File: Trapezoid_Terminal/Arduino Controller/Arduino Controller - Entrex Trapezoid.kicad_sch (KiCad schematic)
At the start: 19 parts, among them J1 Conn_01x19, J10 Conn_01x04, J2 Conn_01x04, J3 Conn_01x08, J4 Conn_01x08, J5 Conn_01x06, J6 Conn_01x04, J7 Conn_01x02, J8 Conn_01x19, J9 Logic 8 CH, U1 74LS04

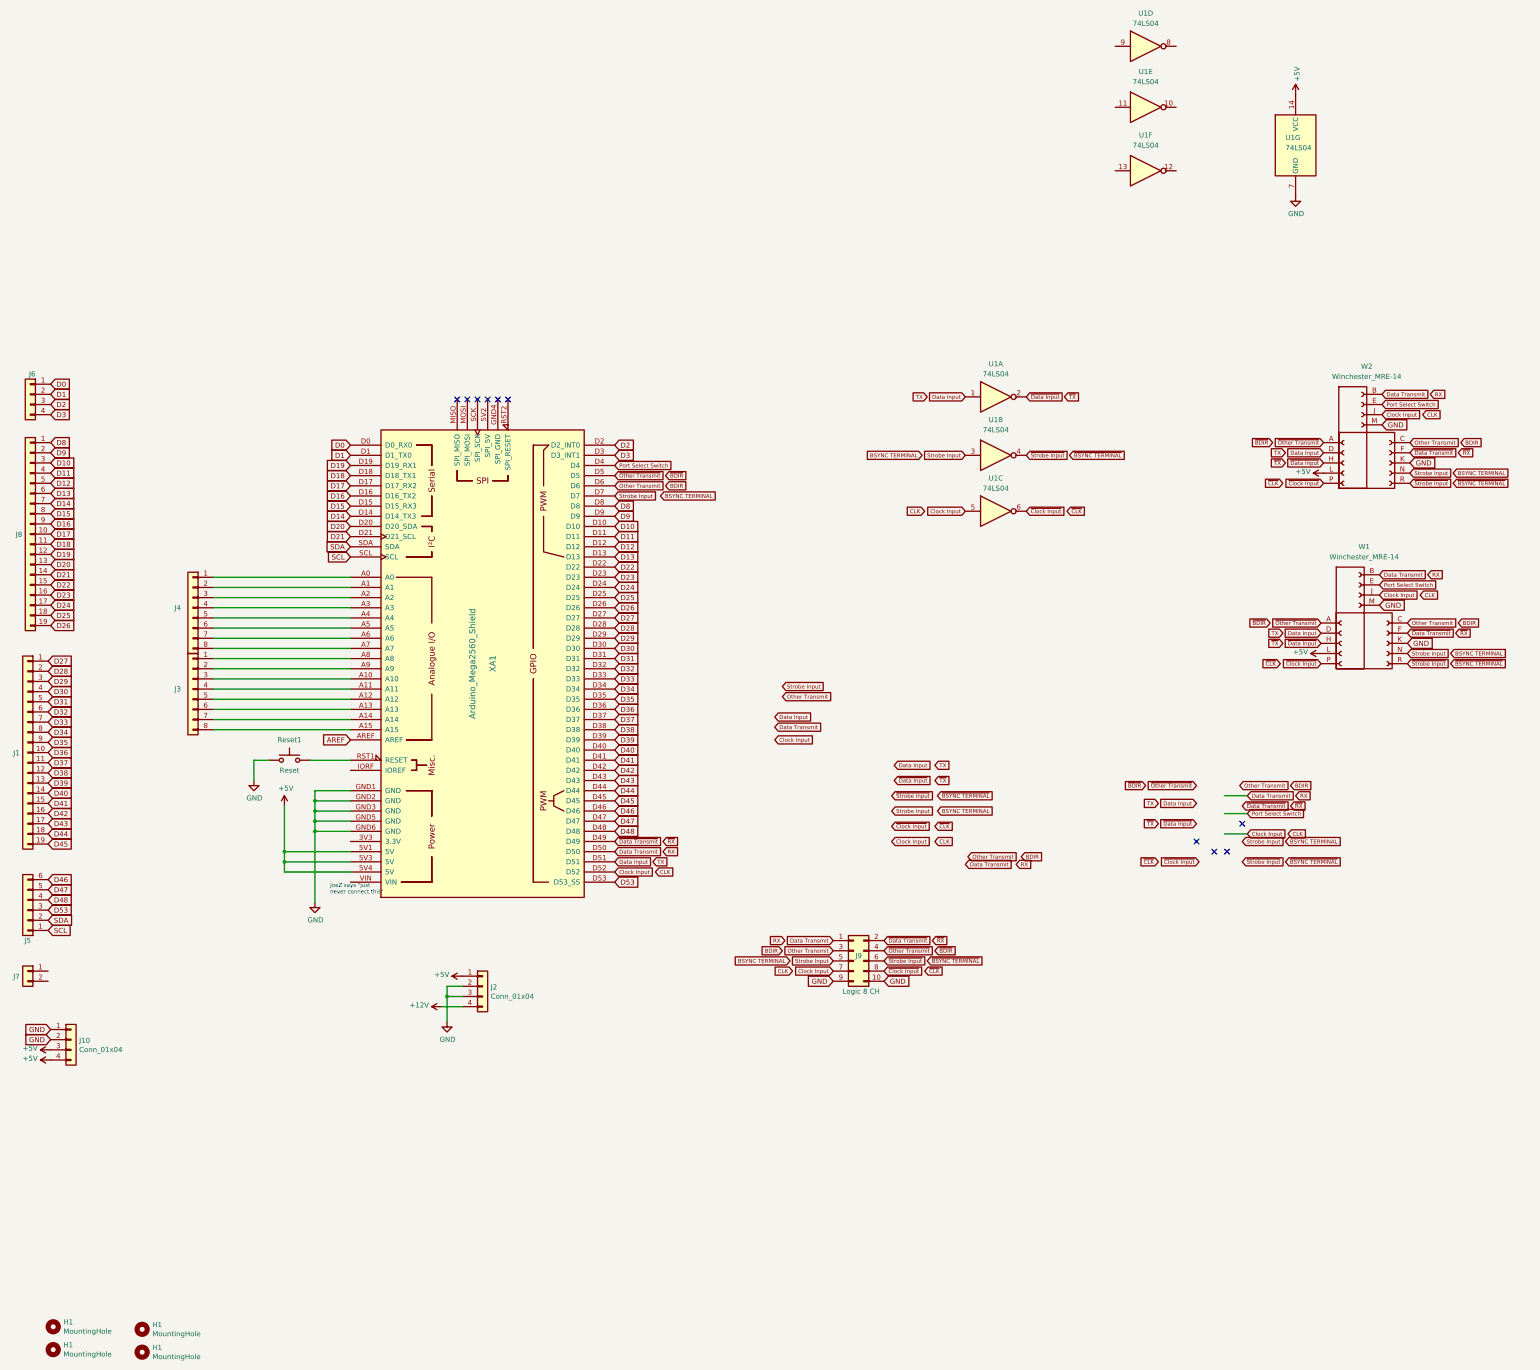
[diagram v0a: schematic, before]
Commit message: Trapezoid Terminal Interface Corrections
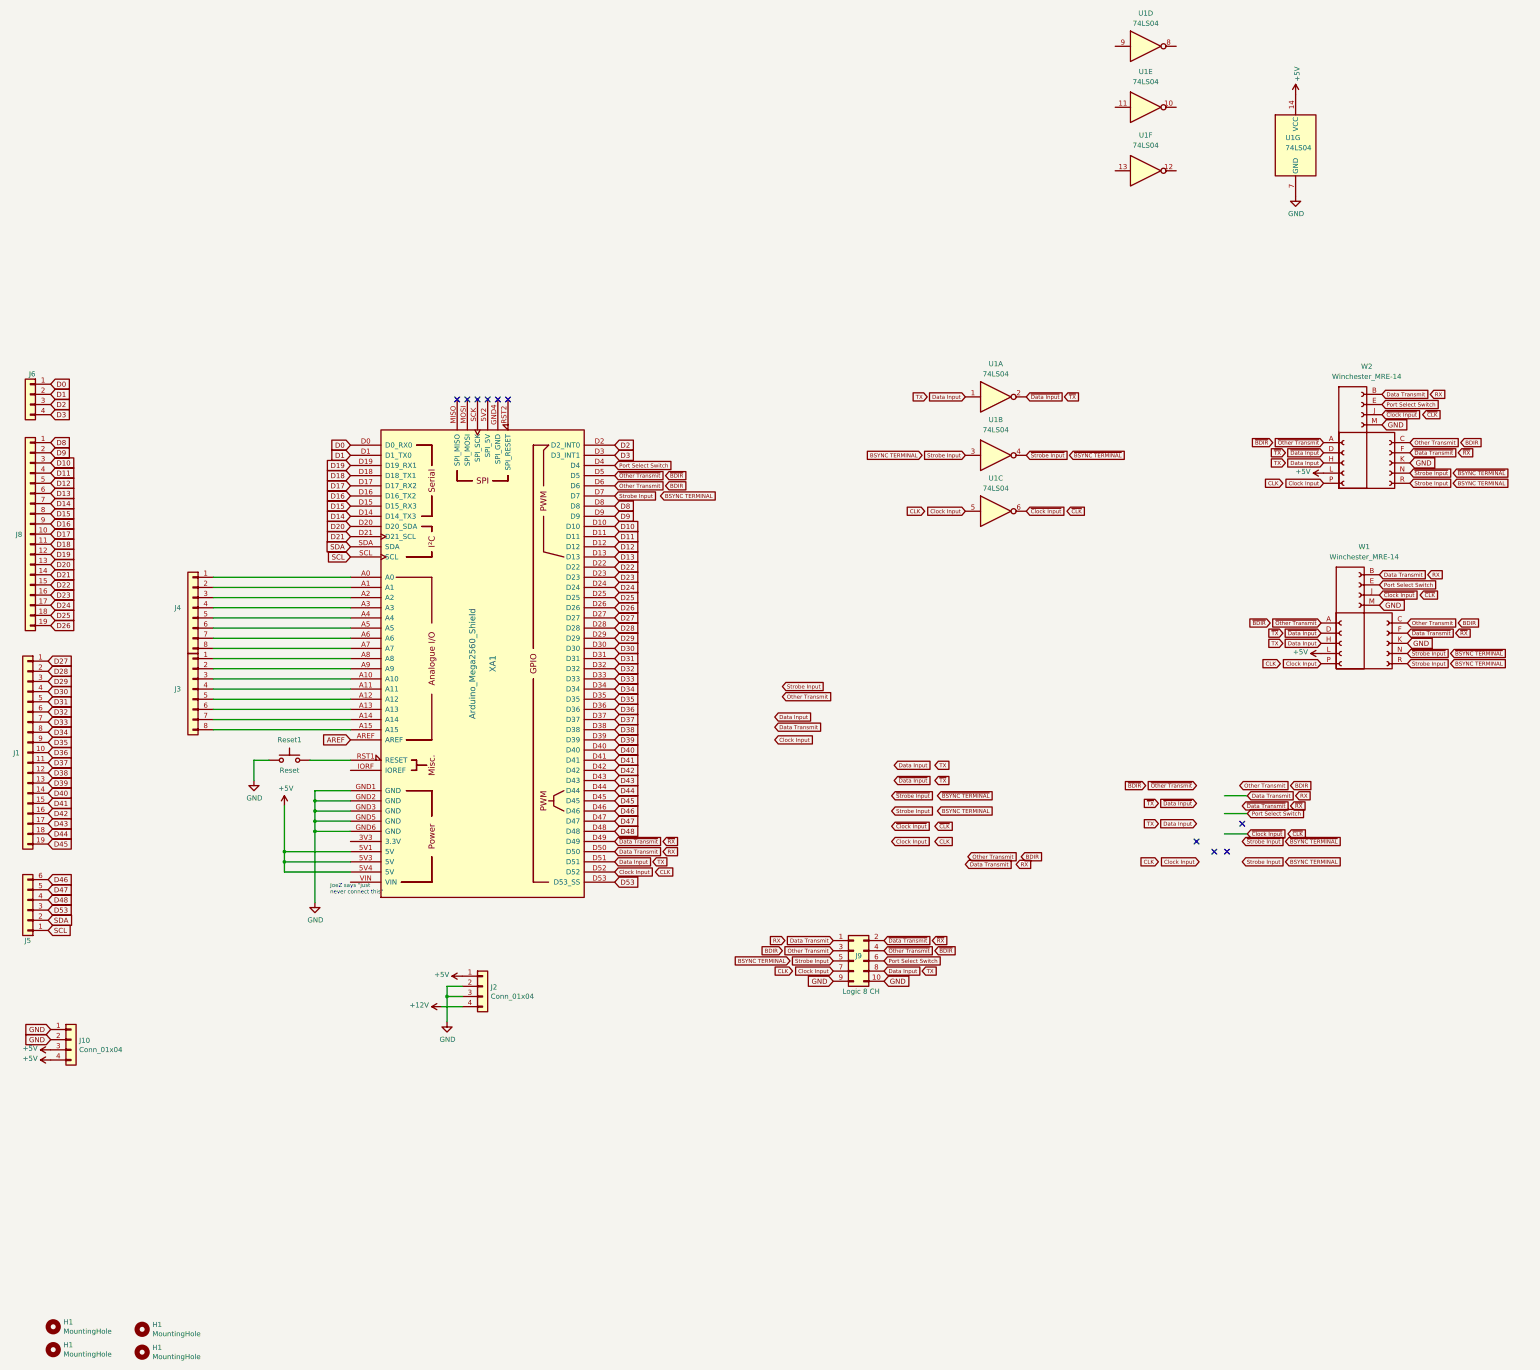
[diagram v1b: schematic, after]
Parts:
- removed J7: Conn_01x02, port_nova:PinHeader_1x02_P2.54mm_Vertical, symbol Connector_Generic:Conn_01x02
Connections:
- net Clock Input: now also W1.P (Pin_5), W2.P (Pin_5); no longer W1.J (Pin_2), W2.J (Pin_2)
- net Data Input: now also J9.8 (Pin_8), W1.H (Pin_3), W2.H (Pin_3); no longer W1.D (Pin_2), W2.D (Pin_2)
- net Port Select Switch: now also J9.6 (Pin_6)
- net Strobe Input: now also W1.R (Pin_1), W2.R (Pin_1); no longer W1.N (Pin_2), W2.N (Pin_2)
- net ~{Clock Input}: now also W1.J (Pin_2), W2.J (Pin_2); no longer J9.8 (Pin_8), W1.P (Pin_5), W2.P (Pin_5)
- net ~{Data Input}: now also W1.D (Pin_2), W2.D (Pin_2); no longer W1.H (Pin_3), W2.H (Pin_3)
- net ~{Strobe Input}: now also W1.N (Pin_2), W2.N (Pin_2); no longer J9.6 (Pin_6), W1.R (Pin_1), W2.R (Pin_1)
